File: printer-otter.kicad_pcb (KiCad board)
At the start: 2 copper layers, 36 x 32 mm, 49 parts, among them J1 USB, J2 Printer, J4 Encoder, J5 UART, J6 Analog, Q1 Q_NMOS_GSD, Q2 Q_PMOS_GSD, Q3 Q_NMOS_GSD, Q4 Q_PMOS_GSD, SW1 Down, U1 MT3608, U2 STM32F072C8Ux, U3 AP2204R-3.3, U4 USBLC6-4SC6, U5 L78L09_SOT89, U6 4504, U7 4504

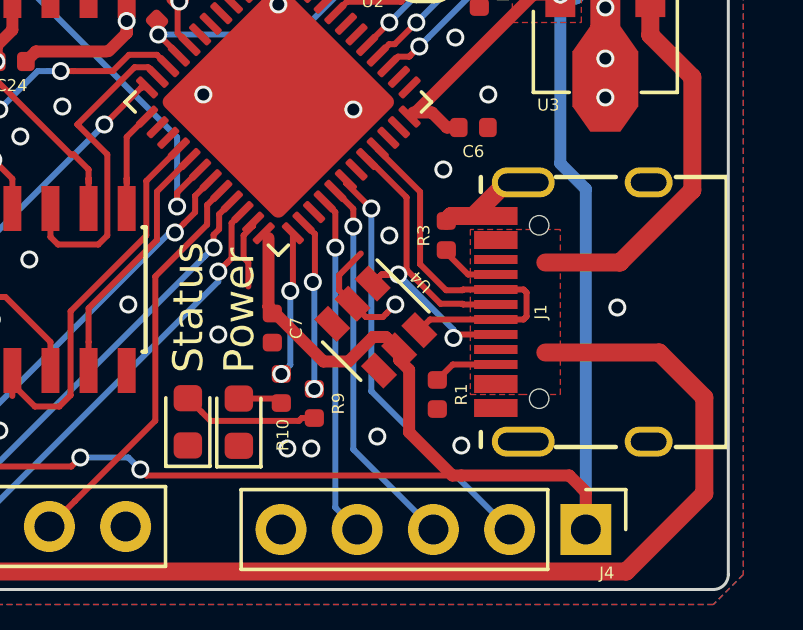
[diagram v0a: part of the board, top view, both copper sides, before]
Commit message: fixed USB-C plug and updated fiels
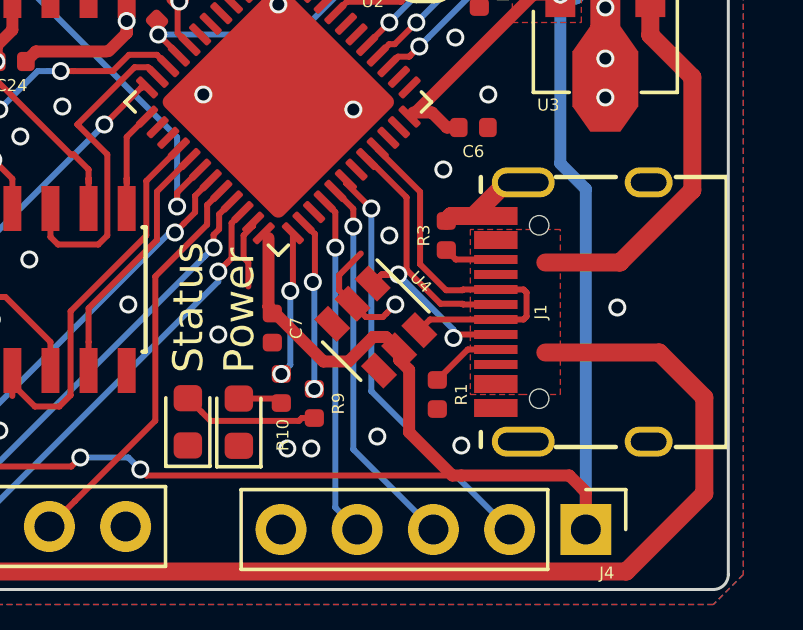
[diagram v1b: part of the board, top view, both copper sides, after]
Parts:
- J1: footprint badgelib:USB-C 16Pin -> otter:USB-C 16Pin

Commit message: updated kicad files
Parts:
- removed C19: 1uF, Capacitor_SMD:C_0402_1005Metric
- removed JP1: Boot, Jumper:SolderJumper-2_P1.3mm_Open_RoundedPad1.0x1.5mm
- added C3: 10µF, Capacitor_SMD:CP_Elec_4x3, F.Cu at (126.9, 104.7)
- C1, C18, C2, C21, C22, C23, C24, C4, C5, C6, C7: footprint Capacitor_SMD:C_0402_1005Metric -> Capacitor_SMD:C_0603_1608Metric
- C11, C20: footprint Capacitor_SMD:C_0402_1005Metric -> Capacitor_SMD:C_0805_2012Metric
- R1, R10, R11, R12, R13, R2, R3, R4, R5, R6, R7, R8, R9: footprint Resistor_SMD:R_0402_1005Metric -> Resistor_SMD:R_0603_1608Metric
- moved SW1 20.8 mm to (134.0, 114.6), turned to 90 degrees
- moved C7 19.3 mm to (116.0, 104.6), turned to 180 degrees
- moved J6 18.4 mm to (115.6, 101.9)
- moved C2 16.6 mm to (115.5, 116.6), turned to 90 degrees
- moved U3 15.5 mm to (120.2, 103.5)
- moved C1 12.4 mm to (123.6, 102.5), turned to 270 degrees
- moved R5 9.19 mm to (130.2, 112.1), turned to 0 degrees
- moved U4 8.67 mm to (126.9, 115.0), turned to 90 degrees
- moved C20 8.48 mm to (130.4, 104.8), turned to 90 degrees
- moved C11 7.23 mm to (133.3, 101.9), turned to 180 degrees
- moved C6 6.48 mm to (122.7, 121.0), turned to 180 degrees
- moved C5 5.66 mm to (126.2, 112.3)
- moved L1 4.69 mm to (133.4, 108.8), turned to 180 degrees
- moved D2 4.68 mm to (129.9, 108.9), turned to 270 degrees
- moved R4 4.62 mm to (128.0, 109.8), turned to 270 degrees
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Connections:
- net OLED_SCL renamed Net-(U2-Pad42)
- net OLED_SDA renamed Net-(U2-Pad43)
- J5 pad 2: UART_TX -> INT_IN
- J5 pad 3: UART_RX -> UART_TX
- J5 pad 4: INT_IN -> UART_RX
- R2 pad 2: Net-(JP1-Pad2) -> BTN
- SW1 pad 2: Net-(SW1-Pad2) -> BTN
- U2 pad 14: Net-(U2-Pad14) -> F5
- U2 pad 15: Net-(U2-Pad15) -> F3
- U2 pad 18: F3 -> Net-(U2-Pad18)
- U2 pad 19: F5 -> Net-(U2-Pad19)
- U2 pad 31: Net-(U2-Pad31) -> CSYNC
- U2 pad 44: Net-(JP1-Pad2) -> BTN
- U2 pad 45: Net-(SW1-Pad2) -> BTN
- U2 pad 46: CSYNC -> Net-(U2-Pad46)
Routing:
- net +3V3: track 124.5 -> 0.00 mm, vias 6 -> 0
- net VBUS: track 58.8 -> 0.00 mm
- net 16V: track 49.7 -> 0.00 mm, vias 4 -> 0
- net F3: track 26.0 -> 0.00 mm, vias 2 -> 0
- net F5: track 23.7 -> 0.00 mm, vias 2 -> 0
- net GND: track 21.0 -> 0.00 mm, vias 61 -> 0
- net Net-(SW1-Pad2): track 19.6 -> 0.00 mm, vias 2 -> 0
- net CSYNC: track 18.7 -> 0.00 mm, vias 2 -> 0
- net 9V: track 16.9 -> 0.00 mm, vias 2 -> 0
- net UART_TX: track 16.2 -> 0.00 mm, vias 1 -> 0
- net GPIO_ANALOG0: track 15.5 -> 0.00 mm, vias 1 -> 0
- net D2: track 14.5 -> 0.00 mm, vias 2 -> 0
- net UART_RX: track 14.2 -> 0.00 mm, vias 1 -> 0
- net D1: track 14.2 -> 0.00 mm
- net GPIO_ANALOG1: track 14.1 -> 0.00 mm, vias 1 -> 0
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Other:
- outline, holes or cut-outs redrawn
- board text added: "Otter- Printer"
- board text removed: "Otter-Printer"

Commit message: updated Kicad files
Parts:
- removed J6: Analog, Connector_PinHeader_2.54mm:PinHeader_1x05_P2.54mm_Vertical
- moved R9 1.35 mm to (122.8, 125.3)
- moved R10 1.12 mm to (121.3, 124.5)
- moved C7 0.92 mm to (116.8, 104.1), turned to 270 degrees
- moved C6 0.43 mm to (123.1, 121.1)
- moved C5 0.42 mm to (126.1, 111.9), turned to 0 degrees
- moved U1 0.13 mm to (133.2, 104.7)
- moved U7 0.11 mm to (110.9, 110.1)
- moved C4 0.11 mm to (117.8, 111.1)
- moved U6 0.10 mm to (110.9, 121.8)
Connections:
- R10 pad 1: Net-(R10-Pad1) -> LED_Status
- R9 pad 1: Net-(R9-Pad1) -> LED_Power
- U2 pad 11: S5 -> S3
- U2 pad 12: S2 -> S5
- U2 pad 13: S3 -> S2
- U2 pad 14: F5 -> S4
- U2 pad 15: F3 -> S1
- U2 pad 16: S4 -> F5
- U2 pad 17: S1 -> F3
- U2 pad 18: Net-(U2-Pad18) -> LED_Status
- U2 pad 19: Net-(U2-Pad19) -> LED_Power
- U2 pad 25: Net-(R10-Pad1) -> Net-(U2-Pad25)
- U2 pad 26: Net-(R9-Pad1) -> Net-(U2-Pad26)
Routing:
- net +3V3: track 0.00 -> 96.8 mm, vias 0 -> 5
- net VBUS: track 0.00 -> 71.1 mm, vias 0 -> 7
- net 16V: track 0.00 -> 51.7 mm, vias 0 -> 4
- net F3: track 0.00 -> 32.2 mm, vias 0 -> 4
- net GND: track 0.00 -> 29.4 mm, vias 0 -> 79
- net F5: track 0.00 -> 25.8 mm
- net BTN: track 0.00 -> 24.2 mm, vias 0 -> 2
- net CSYNC: track 0.00 -> 22.0 mm, vias 0 -> 2
- net INT_IN: track 0.00 -> 19.5 mm, vias 0 -> 1
- net UART_TX: track 0.00 -> 19.1 mm, vias 0 -> 1
- net UART_RX: track 0.00 -> 18.3 mm, vias 0 -> 1
- net ENCODER_A: track 0.00 -> 16.3 mm, vias 0 -> 1
- net INDEX: track 0.00 -> 14.6 mm, vias 0 -> 1
- net ENCODER_B: track 0.00 -> 14.6 mm, vias 0 -> 1
- net D2: track 0.00 -> 13.7 mm
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- added copper zone on B.Cu, net VBUS
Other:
- board text added: "Desing by Jan Henrik Hemsing Twitter: @JanHenrikH"
- board text removed: "@JanHenrikH"
- board text removed: "PB3"
- board text removed: "PB4"
- board text removed: "PB5"
